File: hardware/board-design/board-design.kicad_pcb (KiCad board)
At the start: 4 copper layers, 0 parts

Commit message: feat(pcb): draw buck part (WIP)
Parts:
- added C_BOOT1: 0.1uF, Capacitor_SMD:C_0603_1608Metric_Pad1.08x0.95mm_HandSolder, F.Cu at (138.0, 96.1)
- added C_BP_3: 10uF, Custom-lib:CAPC6153X390N, F.Cu at (137.2, 85.0)
- added C_BP_4: 0.1uF, Capacitor_SMD:C_0603_1608Metric_Pad1.08x0.95mm_HandSolder, F.Cu at (132.0, 91.1)
- added C_BP_5: 10uF, Custom-lib:CAPC6153X390N, F.Cu at (130.2, 84.9)
- added C_Comp1: 15nF, Capacitor_SMD:C_0603_1608Metric_Pad1.08x0.95mm_HandSolder, F.Cu at (136.3, 105.7)
- added C_HF1: 100pF, Capacitor_SMD:C_0603_1608Metric_Pad1.08x0.95mm_HandSolder, F.Cu at (137.3, 103.1)
- added C_Vcc1: 4.7uF, Capacitor_SMD:C_0805_2012Metric_Pad1.18x1.45mm_HandSolder, F.Cu at (133.9, 100.0)
- added C_out1: 47uF, Custom-lib:CAPC6075X690N, F.Cu at (158.7, 87.0)
- added C_out2: 47uF, Custom-lib:CAPC6075X690N, F.Cu at (169.0, 96.0)
- added C_out3: 47uF, Custom-lib:CAPC6075X690N, F.Cu at (158.7, 96.0)
- added C_out4: 47uF, Custom-lib:CAPC6075X690N, F.Cu at (169.0, 87.0)
- added L1: 1.5uH, Custom-lib:WE-LHMI_7030, F.Cu at (145.2, 91.5)
- added Q_HIGH_1: Q_NMOS_DGS, Package_SON:VSONP-8-1EP_5x6_P1.27mm, F.Cu at (136.8, 92.1)
- added Q_HIGH_2: Q_NMOS_DGS, Package_SON:VSONP-8-1EP_5x6_P1.27mm, F.Cu at (144.2, 98.7)
- added Rcomp1: 6.04k, Resistor_SMD:R_0603_1608Metric_Pad0.98x0.95mm_HandSolder, F.Cu at (135.4, 103.2)
- added Rs1: 3m, Resistor_SMD:R_0612_1632Metric_Pad1.18x3.40mm_HandSolder, F.Cu at (152.0, 91.6)
- added Rt1: 53.6k, Resistor_SMD:R_0603_1608Metric_Pad0.98x0.95mm_HandSolder, F.Cu at (134.1, 98.0)
- added U1: LM25139, Package_DFN_QFN:VQFN-16-1EP_3x3mm_P0.5mm_EP1.68x1.68mm, F.Cu at (138.1, 99.2)
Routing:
- net /DC-DC-Buck-Converter/V_OUT: track 0.00 -> 31.9 mm
- net Net-(U1-ISNS): track 0.00 -> 30.7 mm
- net /DC-DC-Buck-Converter/Vcc: track 0.00 -> 8.13 mm, vias 0 -> 2
- net Net-(Q_HIGH_1-G): track 0.00 -> 6.85 mm
- net Net-(Q_HIGH_1-S): track 0.00 -> 4.24 mm
- net /DC-DC-Buck-Converter/V_INPUT: track 0.00 -> 3.88 mm
- net Net-(U1-COMP): track 0.00 -> 3.46 mm
- net Net-(Q_HIGH_2-G): track 0.00 -> 3.27 mm
- net Net-(U1-RT): track 0.00 -> 1.96 mm
- net Net-(U1-CBOOT): track 0.00 -> 1.95 mm
- net Net-(C_Comp1-Pad2): track 0.00 -> 1.66 mm
- added copper zone on F.Cu, net Net-(Q_HIGH_1-S)

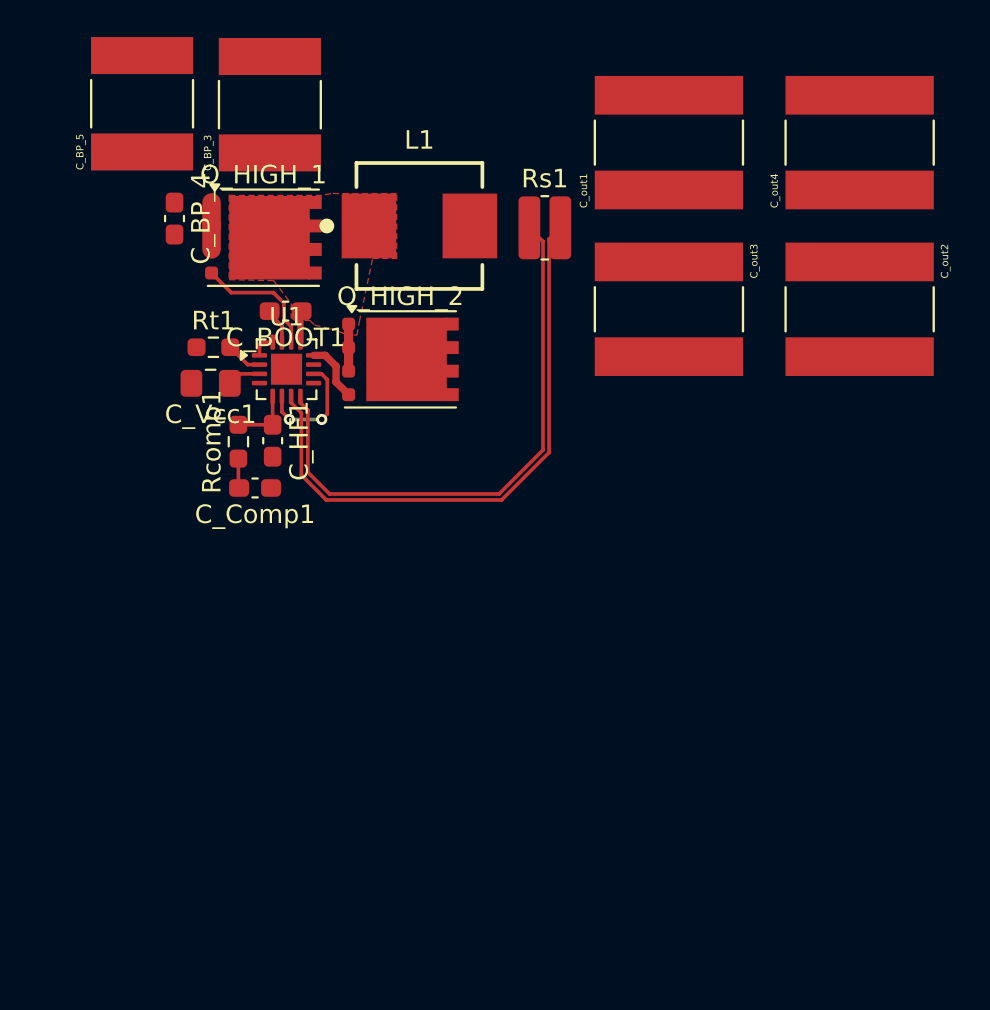
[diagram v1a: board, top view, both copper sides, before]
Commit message: feat(pcb): complate the buck stage
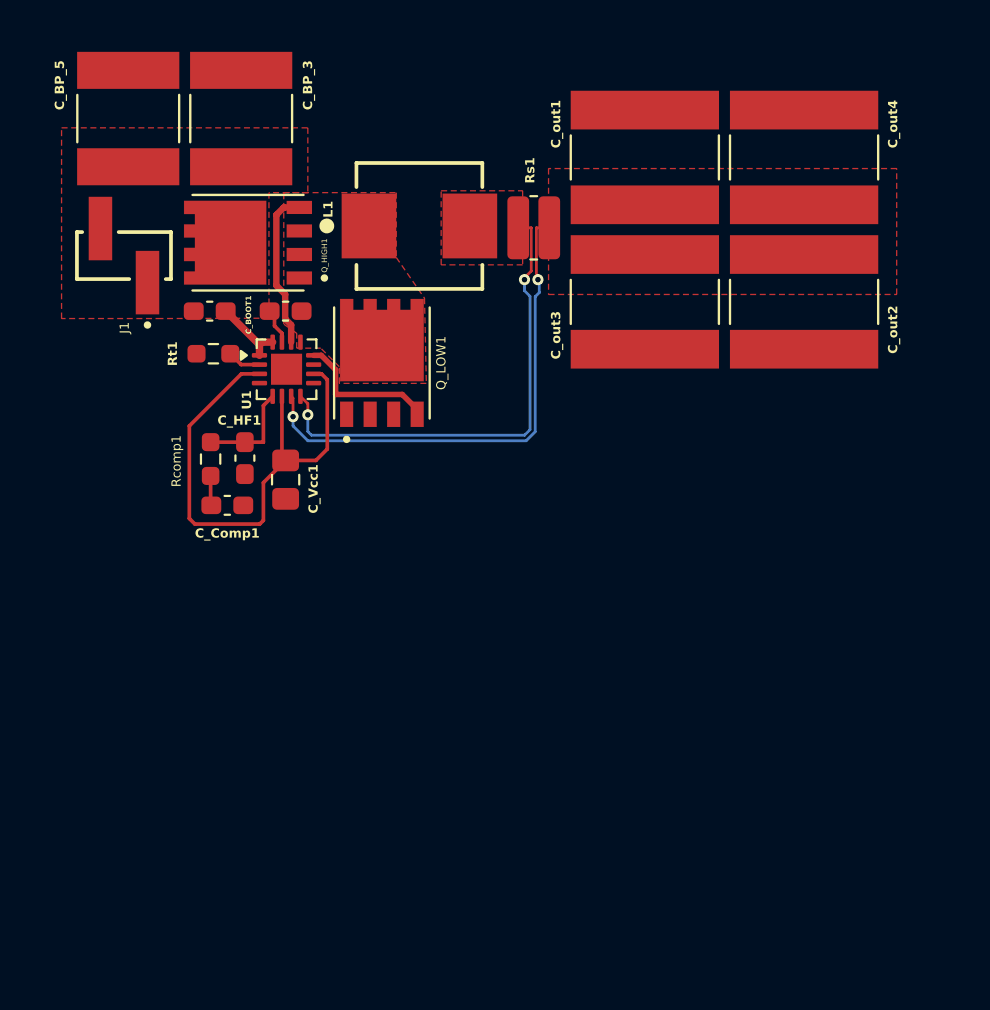
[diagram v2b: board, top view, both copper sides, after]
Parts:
- removed Q_HIGH_1, Q_HIGH_2: Q_NMOS_DGS, Package_SON:VSONP-8-1EP_5x6_P1.27mm
- added J1: Conn_01x02_Pin, Custom-lib:SAMTEC_TSM-102-01-X-SV, F.Cu at (129.3, 93.1)
- added Q_HIGH1: CSD19532Q5B, Custom-lib:TRANS_CSD19532Q5B, F.Cu at (136.0, 92.4)
- added Q_LOW1: CSD19532Q5B, Custom-lib:TRANS_CSD19532Q5B, F.Cu at (143.2, 98.9)
- moved C_Vcc1 6.59 mm to (138.0, 105.2), turned to -90 degrees
- moved C_BP_4 5.35 mm to (133.9, 96.1), turned to 180 degrees
- moved C_out4 3.10 mm to (166.0, 87.8)
- moved C_out2 3.03 mm to (166.0, 95.6)
- moved C_Comp1 1.77 mm to (134.8, 106.6)
- moved C_HF1 1.77 mm to (135.8, 104.0)
- moved Rcomp1 1.77 mm to (133.9, 104.1)
- moved C_BP_3 1.72 mm to (135.6, 85.7)
- moved C_out1 1.53 mm to (157.4, 87.8)
- moved C_out3 1.36 mm to (157.4, 95.6)
- moved C_BP_5 1.10 mm to (129.5, 85.7)
- moved Rs1 0.60 mm to (151.4, 91.6)
- moved Rt1 0.35 mm to (134.1, 98.4)
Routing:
- net /DC-DC-Buck-Converter/Vcc: track 8.13 -> 28.6 mm, vias 2 -> 0
- net Net-(U1-ISNS): track 30.7 -> 26.2 mm, vias 0 -> 2
- net Net-(U1-LO): track 3.27 -> 7.85 mm
- net /DC-DC-Buck-Converter/V_OUT: track 31.9 -> 27.5 mm, vias 0 -> 2
- net Net-(U1-SW): track 4.24 -> 0.09 mm
- net Net-(U1-COMP): track 3.46 -> 5.53 mm
- net Net-(U1-HO): track 6.85 -> 8.61 mm
- added copper zone on F.Cu, net /DC-DC-Buck-Converter/V_INPUT
- added copper zone on F.Cu, net /DC-DC-Buck-Converter/V_OUT
- added copper zone on F.Cu, net Net-(U1-ISNS)

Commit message: feat(pcb): complate the pcb design
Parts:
- added C_STM_1: 0.1uF, Capacitor_SMD:C_0603_1608Metric_Pad1.08x0.95mm_HandSolder, F.Cu at (146.4, 118.4)
- added C_STM_2: 0.1uF, Capacitor_SMD:C_0603_1608Metric_Pad1.08x0.95mm_HandSolder, F.Cu at (146.4, 120.4)
- added C_STM_3: 0.1uF, Capacitor_SMD:C_0603_1608Metric_Pad1.08x0.95mm_HandSolder, F.Cu at (146.4, 116.8)
- added C_STM_4: 10uF, Custom-lib:CAPC6153X390N, F.Cu at (145.1, 112.1)
- added C_STM_5: 10uF, Custom-lib:CAPC6153X390N, B.Cu at (168.8, 126.4)
- added C_STM_6: 0.1uF, Capacitor_SMD:C_0603_1608Metric_Pad1.08x0.95mm_HandSolder, B.Cu at (165.0, 124.2)
- added C_STM_7: 10uF, Custom-lib:CAPC6153X390N, B.Cu at (155.6, 105.9)
- added C_STM_8: 0.1uF, Capacitor_SMD:C_0603_1608Metric_Pad1.08x0.95mm_HandSolder, B.Cu at (151.8, 108.1)
- added D1: D_TVS, Diode_SMD:D_SMA, F.Cu at (141.1, 119.4)
- added D2: D_TVS, Diode_SMD:D_SMA, F.Cu at (162.0, 114.6)
- added D3: D_TVS, Diode_SMD:D_SMA, F.Cu at (158.4, 114.6)
- added J2: Conn_02x05_Odd_Even, Custom-lib:SAMTEC_FTE-105-01-G-DV, F.Cu at (159.5, 120.5)
- added R_OpenDrain1: 4.7k, Resistor_SMD:R_0603_1608Metric_Pad0.98x0.95mm_HandSolder, F.Cu at (149.1, 112.7)
- added R_OpenDrain2: 4.7k, Resistor_SMD:R_0603_1608Metric_Pad0.98x0.95mm_HandSolder, F.Cu at (150.7, 112.7)
- added SW1: SW_Push, Button_Switch_SMD:SW_SPST_B3U-1000P-B, F.Cu at (145.7, 122.9)
- added U2: ER_OLEDM0.91_1x-I2C, Display:ER_OLEDM0.91_1x-I2C, B.Cu at (170.1, 120.0)
- added U3: STM32C031C6Ux, Package_DFN_QFN:QFN-48-1EP_7x7mm_P0.5mm_EP5.6x5.6mm, F.Cu at (152.3, 118.6)
- added U4: BMP180, Custom-lib:GY-68, B.Cu at (165.3, 92.7)
- moved C_BOOT1 1.96 mm to (138.5, 98.0)
- moved C_BP_4 1.96 mm to (134.4, 98.0)
- moved C_HF1 1.96 mm to (136.3, 105.9)
- moved C_out1 1.96 mm to (157.9, 89.7)
- moved C_out2 1.96 mm to (166.5, 97.5)
- moved C_out3 1.96 mm to (157.9, 97.5)
- moved C_out4 1.96 mm to (166.5, 89.7)
- moved J1 1.96 mm to (129.8, 95.0)
- moved L1 1.96 mm to (145.7, 93.4)
- moved Q_HIGH1 1.96 mm to (136.5, 94.3)
- moved Rs1 1.96 mm to (151.9, 93.5)
- moved U1 1.96 mm to (138.6, 101.1)
- moved C_BP_3 1.96 mm to (136.1, 87.6)
- moved C_BP_5 1.96 mm to (130.0, 87.6)
- moved C_Comp1 1.96 mm to (135.3, 108.5)
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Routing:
- net GND: track 0.00 -> 54.1 mm, vias 0 -> 81
- net /DC-DC-Buck-Converter/V_OUT: track 27.5 -> 76.4 mm, vias 2 -> 12
- net Net-(U2-SDA): track 0.00 -> 32.9 mm, vias 0 -> 1
- net Net-(U2-SCL): track 0.00 -> 27.1 mm, vias 0 -> 1
- net /STM32/NRST: track 0.00 -> 22.9 mm
- net Net-(D2-A2): track 0.00 -> 11.8 mm
- net /DC-DC-Buck-Converter/Vcc: track 28.6 -> 18.5 mm, vias 0 -> 2
- net Net-(D3-A2): track 0.00 -> 6.45 mm
- net /DC-DC-Buck-Converter/V_INPUT: track 4.21 -> 6.74 mm, vias 0 -> 1
- added copper zone on In2.Cu, net /DC-DC-Buck-Converter/V_INPUT
- added copper zone on In2.Cu, net /DC-DC-Buck-Converter/V_OUT
- added copper zone on B.Cu, net GND
- added copper zone on F.Cu, net GND
- added copper zone on In1.Cu, net GND
- added copper zone on In2.Cu, net GND
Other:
- board outline added: 49 x 50 mm
- board text added: "STM32 Synchronous Buck & Sensor Node Ahmet Duran Tek"
